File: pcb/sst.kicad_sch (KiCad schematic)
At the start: 35 parts, among them X1 CONN_PWR, X2 CONN_INPUTS, X3 CONN_SPI, X4 CONN_INPUTS, X5 CONN_I2C

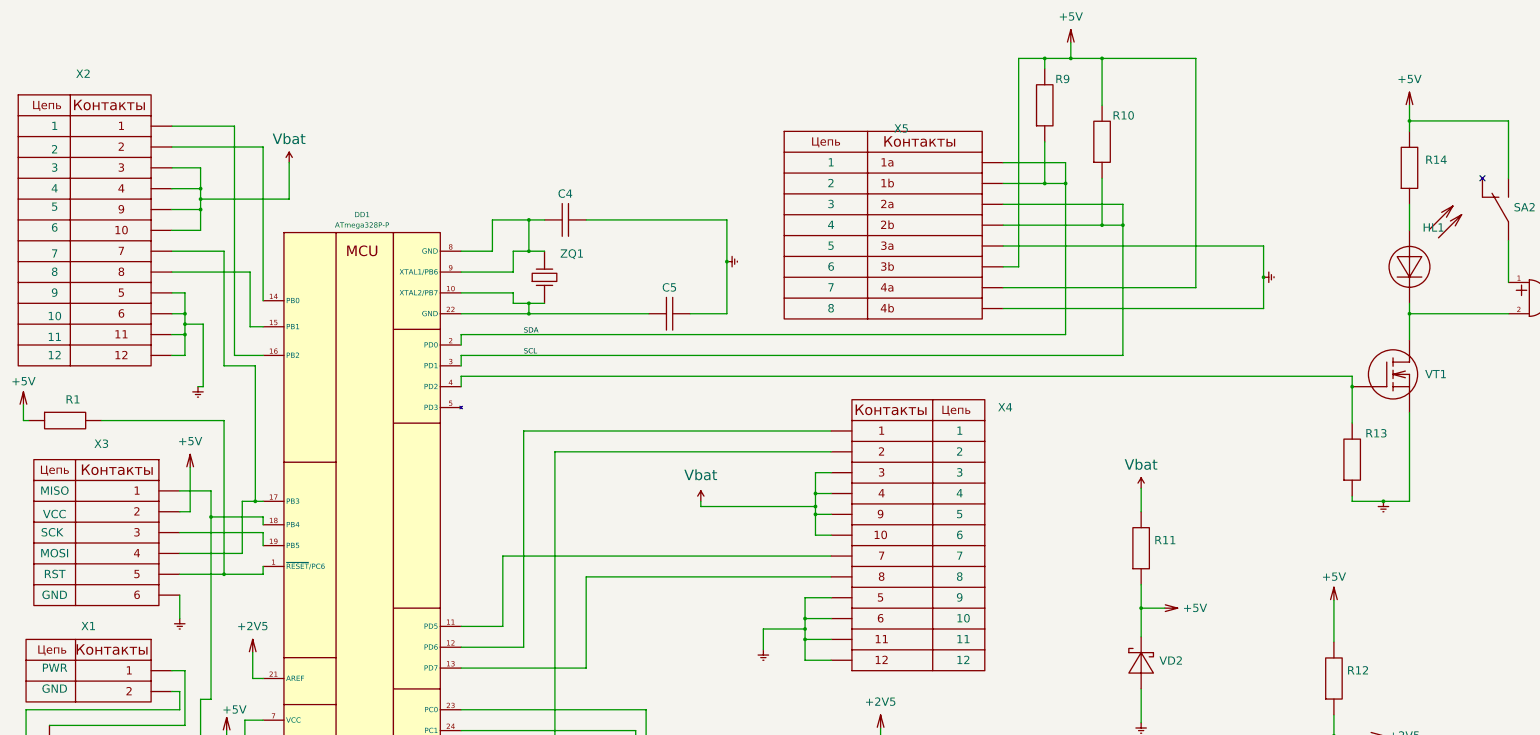
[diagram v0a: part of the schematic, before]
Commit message: Одинаковые надписи и больше подписанных цепей
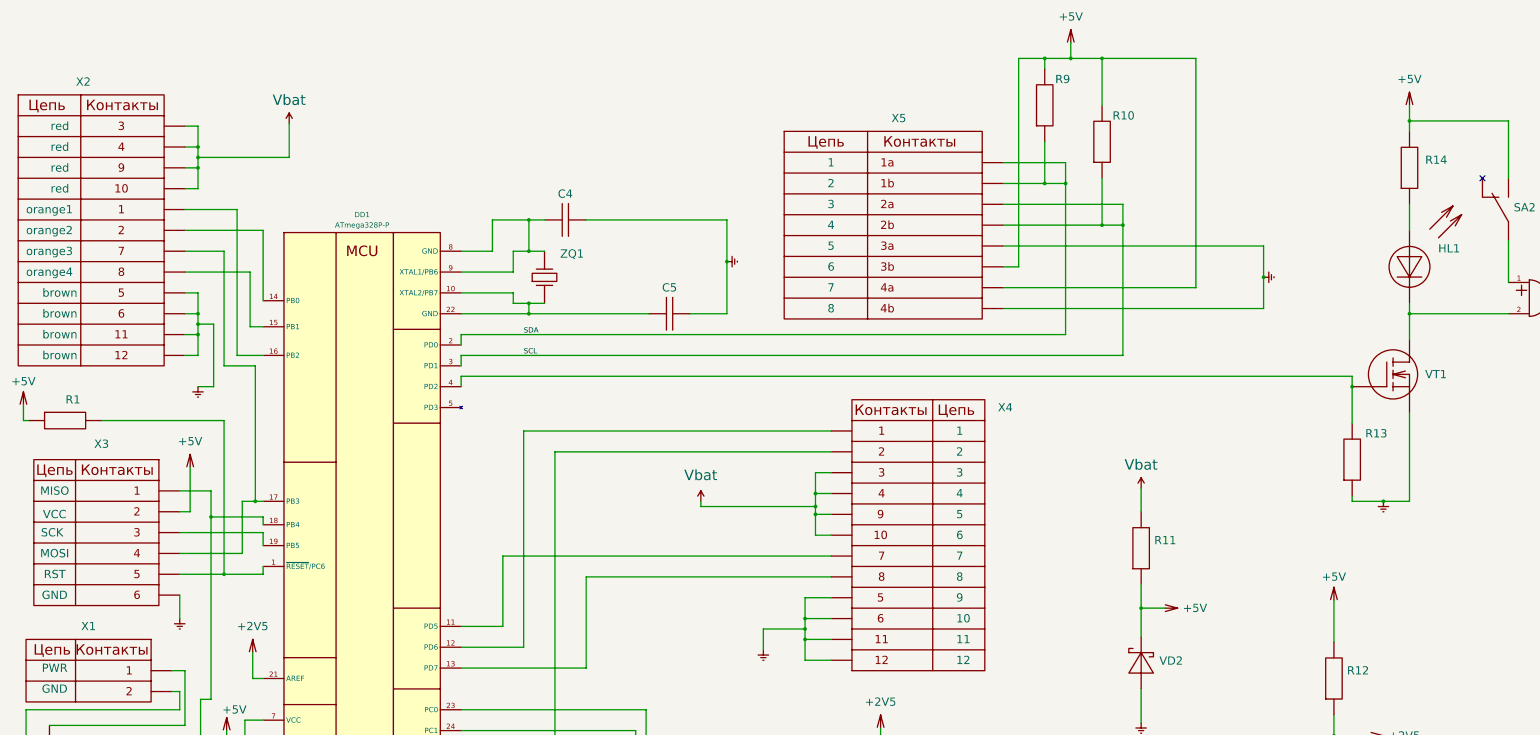
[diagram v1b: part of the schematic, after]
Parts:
- X2: PIN1 1 -> orange1; PIN10 10 -> red; PIN11 11 -> brown; PIN12 12 -> brown; PIN2 2 -> orange2; PIN3 3 -> red; PIN4 4 -> red; PIN5 5 -> brown; PIN6 6 -> brown; PIN7 7 -> orange3; PIN8 8 -> orange4; PIN9 9 -> red
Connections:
- net Vbat: now also X2.1, X2.2; no longer X2.5, X2.6
- net at DD1.14 (PB0): now also X2.6; no longer X2.2
- net at DD1.16 (PB2): now also X2.5; no longer X2.1
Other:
- moved on the sheet: X1, X2, X3, X4

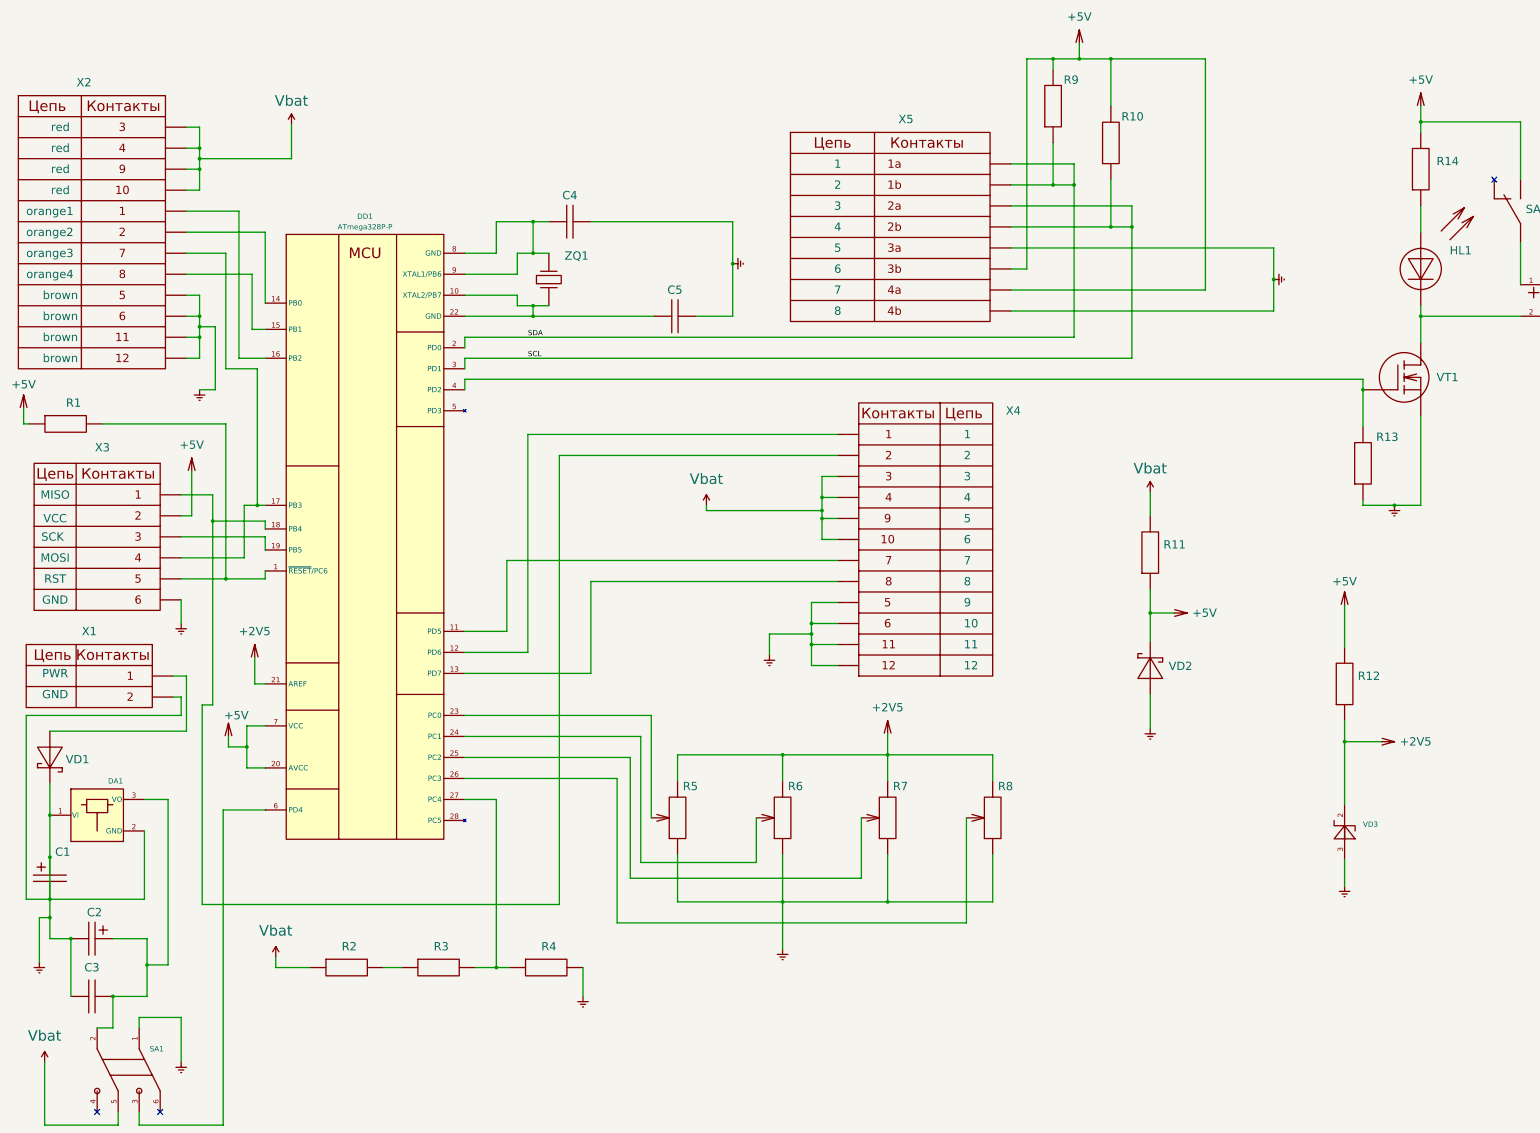
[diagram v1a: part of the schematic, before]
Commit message: Резистор, символ заземления, подписаны цепи, библиотека для струкурной схемы.
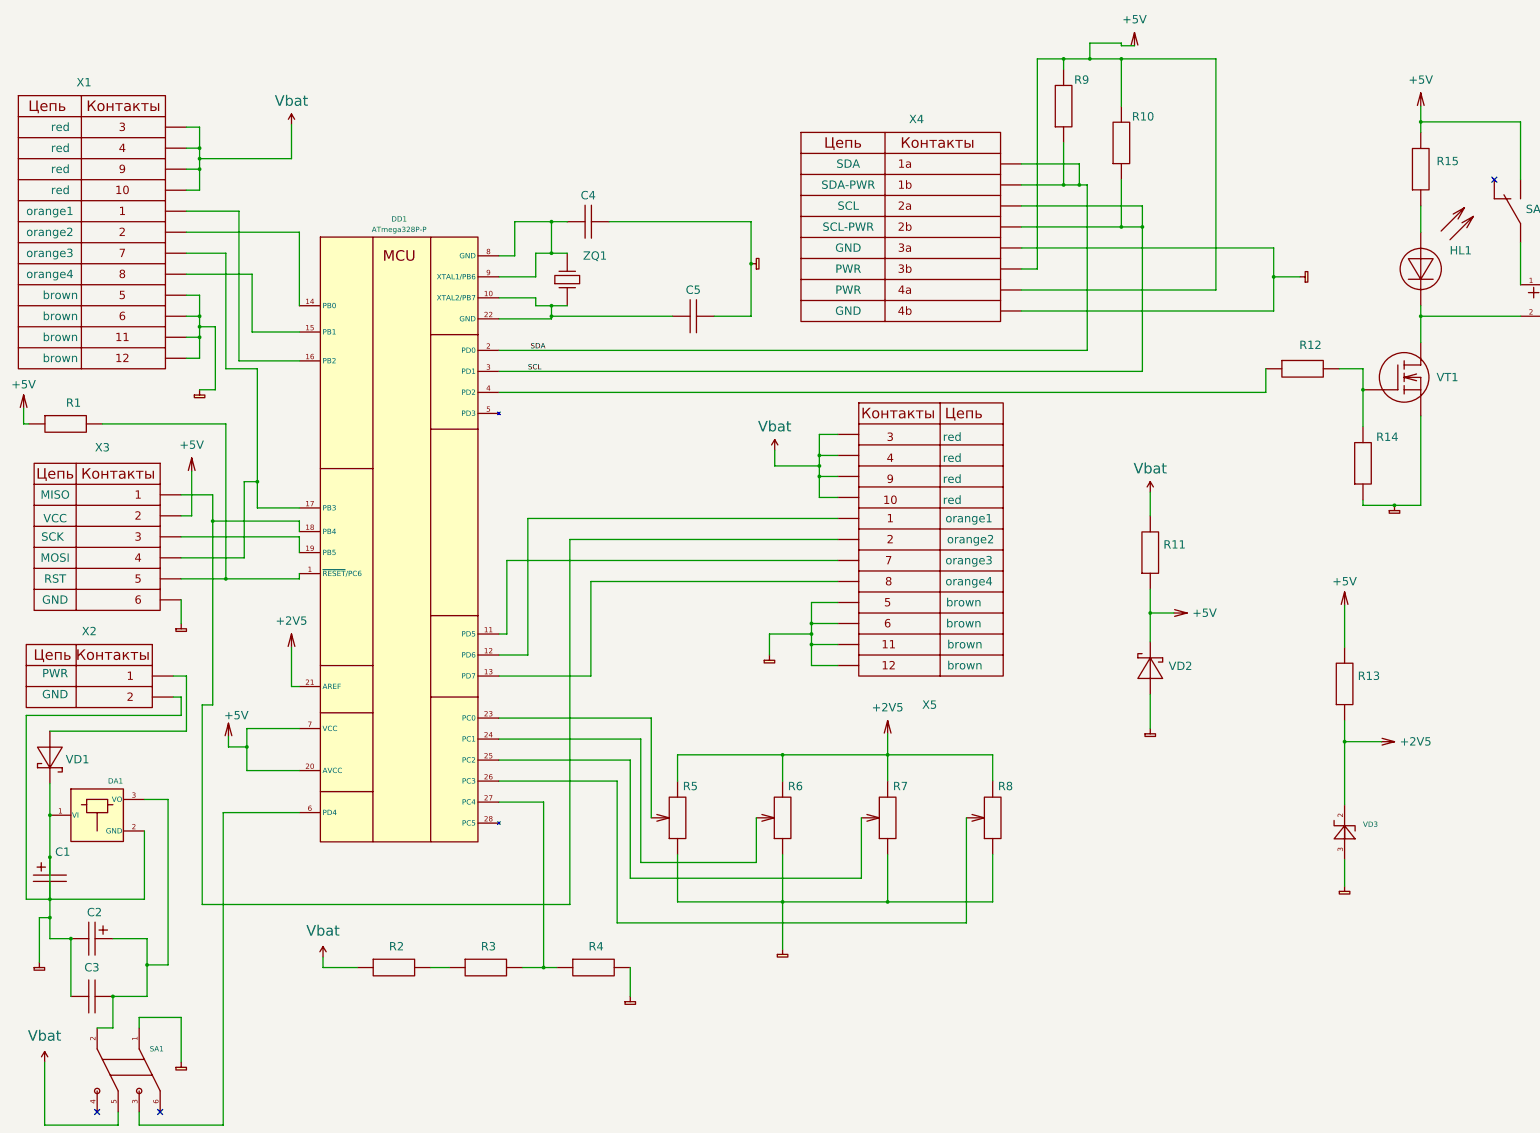
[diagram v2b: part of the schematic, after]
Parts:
- added R12: 22, symbol Device_GOST:R
- X4: renamed from X5; PIN1 1 -> SDA; PIN2 2 -> SDA-PWR; PIN3 3 -> SCL; PIN4 4 -> SCL-PWR; PIN5 5 -> GND; PIN6 6 -> PWR; PIN7 7 -> PWR; PIN8 8 -> GND
- X5: renamed from X4; PIN1 1 -> orange1; PIN10 10 -> red; PIN11 11 -> brown; PIN12 12 -> brown; PIN2 2 -> orange2; PIN3 3 -> red; PIN4 4 -> red; PIN5 5 -> brown; PIN6 6 -> brown; PIN7 7 -> orange3; PIN8 8 -> orange4; PIN9 9 -> red
- renumbered R12 to R13, R13 to R14, R14 to R15, X2 to X1, X1 to X2
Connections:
- net Vbat: now also X5.1, X5.2; no longer X5.5, X5.6
- net at DD1.12 (PD6): now also X5.5; no longer X5.1
- net at DD1.18 (PB4), X3.1: now also X5.6; no longer X5.2
- net at R14.2, VT1.2 (G1): now also R12.2; no longer DD1.4 (PD2)
- new net: DD1.4 (PD2), R12.1
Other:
- moved on the sheet: C4, C5, DD1, R10, R2, R3, R4, R9, X4, ZQ1

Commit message: трассировка печатной платы
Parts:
- C1, C2: footprint (none) -> Capacitor_THT:CP_Radial_D13.0mm_P5.00mm
- C3: footprint (none) -> Capacitor_THT:C_Radial_D10.0mm_H12.5mm_P5.00mm
- C4, C5: footprint (none) -> Capacitor_THT:C_Radial_D6.3mm_H7.0mm_P2.50mm
- DD1: value ATmega328P-P -> Микроконтроллер ATmega328P-P
- HA1: footprint (none) -> Buzzer_Beeper:Buzzer_12x9.5RM7.6
- HL1: footprint (none) -> LED_THT:LED_D3.0mm
- R1, R10, R15, R2, R3, R4, R9: footprint (none) -> Resistor_THT:R_Axial_DIN0207_L6.3mm_D2.5mm_P7.62mm_Horizontal
- R11, R12, R13, R14: footprint (none) -> Resistor_THT:R_Axial_DIN0204_L3.6mm_D1.6mm_P5.08mm_Horizontal
- R5, R6, R7, R8: footprint (none) -> Potentiometer_THT:Potentiometer_TT_P0915N
- SA1: value ~ -> SA_DPDT; footprint (none) -> Button_Switch_THT:SW_CK_JS202011AQN_DPDT_Angled
- SA2: footprint (none) -> Button_Switch_THT:SW_Slide_SPDT_Angled_CK_OS102011MA1Q
- VD1: footprint (none) -> Diode_THT:D_DO-41_SOD81_P7.62mm_Horizontal
- VD2: footprint (none) -> Diode_THT:D_DO-35_SOD27_P7.62mm_Horizontal
- X1, X5: footprint (none) -> Connector_PinHeader_2.54mm:PinHeader_2x06_P2.54mm_Horizontal
- X2: footprint (none) -> Connector_BarrelJack:BarrelJack_SwitchcraftConxall_RAPC10U_Horizontal
- X3: footprint (none) -> Connector_PinHeader_1.00mm:PinHeader_2x03_P1.00mm_Horizontal
- X4: footprint (none) -> Connector_PinSocket_1.27mm:PinSocket_2x04_P1.27mm_Vertical
- ZQ1: footprint (none) -> Crystal:Crystal_HC49-U_Vertical
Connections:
- net GND: now also VD3.1
- net at HA1.2 (-), HL1.1 (K): now also VT1.3 (D1); no longer VT1.6 (D1)

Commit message: значения комопнентов на Э3 для эксперементов с генерацией ПЭ3
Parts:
- DD1: value Микроконтроллер ATmega328P-P -> Микроконтроллер ATmega328P
- R1, R10, R2, R3, R4, R9: value 10к -> резистор 10к 0,25Вт
- R11, R12: value 22 -> резистор 22 0,25Вт
- R13, R15: value 1к -> 1к 0,25Вт
- R5, R6, R7, R8: value 10к -> потенциометр 10к 0,25Вт
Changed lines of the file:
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@@
 			)
 		)
-		(property "Value" "10к"
+		(property "Value" "резистор 10к 0,25Вт"
 			(at 145.415 236.22 0)
 			(effects
@@
 			)
 		)
-		(property "Value" "10к"
+		(property "Value" "потенциометр 10к 0,25Вт"
 			(at 212.725 202.565 90)
 			(effects
@@
 			)
 		)
-		(property "Value" "10к"
+		(property "Value" "резистор 10к 0,25Вт"
 			(at 171.45 236.22 0)
 			(effects
@@
 			)
 		)
-		(property "Value" "10к"
+		(property "Value" "потенциометр 10к 0,25Вт"
 			(at 187.325 202.565 90)
 			(effects
@@
 			)
 		)
-		(property "Value" "10к"
+		(property "Value" "потенциометр 10к 0,25Вт"
 			(at 238.125 202.565 90)
 			(effects
@@
 			)
 		)
-		(property "Value" "10к"
+		(property "Value" "резистор 10к 0,25Вт"
 			(at 44.45 106.68 0)
 			(effects
@@
 			)
 		)
-		(property "Value" "22"
+		(property "Value" "резистор 22 0,25Вт"
 			(at 300.99 142.875 90)
 			(effects
@@
 			)
 		)
-		(property "Value" "10к"
+		(property "Value" "резистор 10к 0,25Вт"
 			(at 123.19 236.22 0)
 			(effects
@@
 			)
 		)
-		(property "Value" "10к"
+		(property "Value" "резистор 10к 0,25Вт"
 			(at 280.67 31.115 90)
 			(effects
@@
 			)
 		)
-		(property "Value" "1к"
+		(property "Value" "1к 0,25Вт"
 			(at 347.98 174.625 90)
 			(effects
@@
 			)
 		)
-		(property "Value" "Микроконтроллер ATmega328P-P"
+		(property "Value" "Микроконтроллер ATmega328P"
 			(at 116.205 62.865 0)
 			(effects
@@
 			)
 		)
-		(property "Value" "10к"
+		(property "Value" "потенциометр 10к 0,25Вт"
 			(at 263.525 202.565 90)
 			(effects
@@
 			)
 		)
-		(property "Value" "1к"
+		(property "Value" "1к 0,25Вт"
 			(at 367.03 50.165 90)
 			(effects
@@
 			)
 		)
-		(property "Value" "22"
+		(property "Value" "резистор 22 0,25Вт"
 			(at 334.645 91.44 0)
 			(effects
@@
 			)
 		)
-		(property "Value" "10к"
+		(property "Value" "резистор 10к 0,25Вт"
 			(at 294.64 40.005 90)
 			(effects

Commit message: поменял значения на принципиальной схеме
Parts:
- C2: value 10мк -> 10мк 16В
- R1, R10, R2, R3, R4, R9: value резистор 10к 0,25Вт -> 10к 0,25Вт
- R11: value резистор 22 0,25Вт -> 22 0,25Вт
- R5: value потенциометр 10к 0,25Вт -> 10к 0,25Вт
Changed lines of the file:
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@@
 			)
 		)
-		(property "Value" "резистор 10к 0,25Вт"
+		(property "Value" "10к 0,25Вт"
 			(at 145.415 236.22 0)
 			(effects
@@
 			)
 		)
-		(property "Value" "резистор 10к 0,25Вт"
+		(property "Value" "10к 0,25Вт"
 			(at 171.45 236.22 0)
 			(effects
@@
 			)
 		)
-		(property "Value" "потенциометр 10к 0,25Вт"
+		(property "Value" "10к 0,25Вт"
 			(at 187.325 202.565 90)
 			(effects
@@
 			)
 		)
-		(property "Value" "10мк"
+		(property "Value" "10мк 16В"
 			(at 50.165 230.505 90)
 			(effects
@@
 			)
 		)
-		(property "Value" "резистор 10к 0,25Вт"
+		(property "Value" "10к 0,25Вт"
 			(at 44.45 106.68 0)
 			(effects
@@
 			)
 		)
-		(property "Value" "резистор 22 0,25Вт"
+		(property "Value" "22 0,25Вт"
 			(at 300.99 142.875 90)
 			(effects
@@
 			)
 		)
-		(property "Value" "резистор 10к 0,25Вт"
+		(property "Value" "10к 0,25Вт"
 			(at 123.19 236.22 0)
 			(effects
@@
 			)
 		)
-		(property "Value" "резистор 10к 0,25Вт"
+		(property "Value" "10к 0,25Вт"
 			(at 280.67 31.115 90)
 			(effects
@@
 			)
 		)
-		(property "Value" "резистор 10к 0,25Вт"
+		(property "Value" "10к 0,25Вт"
 			(at 294.64 40.005 90)
 			(effects

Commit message: Изменения по замечаниям с пары
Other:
- title:  «Система тестирования\n сервоприводов квадрокоптера»  ->  «Система тестирования» 
- moved on the sheet: C5, R12, R14, VT1
